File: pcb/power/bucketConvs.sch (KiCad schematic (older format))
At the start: 20 parts, among them U1 LM2840, U2 TS30012

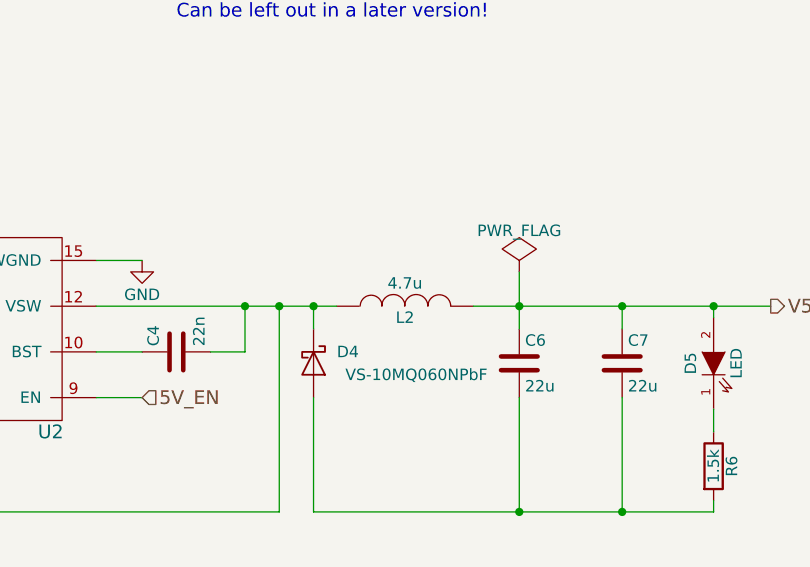
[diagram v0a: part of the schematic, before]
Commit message: Started placing some components.
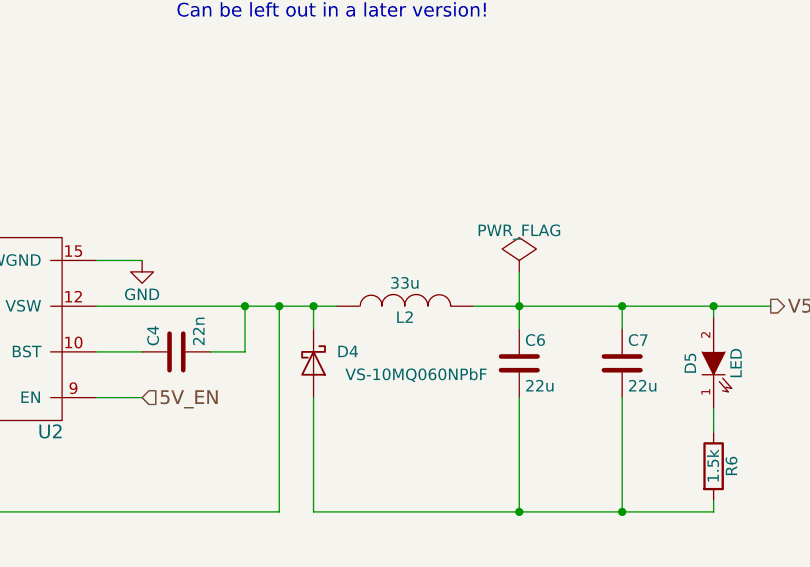
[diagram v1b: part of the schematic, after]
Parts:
- L2: value 4.7u -> 33u; footprint Additional:Taiyo_Yuden_NRS8030_IND -> Additional:Bourns_SRN3015; Digikey 587-2969-1-ND -> SRN3015-330MCT-ND
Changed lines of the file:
@@
 Text Notes 4250 4150 0    60   ~ 0
 Debugging Diode\n-----------------------\nDiode: 1.7 V, 2 mA\nP=2.161 mW\nCan be left out in a later version!
-Wire Wire Line
-	2800 2400 3700 2400
-Wire Wire Line
-	1800 2400 1800 2100
-Wire Wire Line
-	1800 2100 2150 2100
-Wire Wire Line
-	2450 2100 2850 2100
-Wire Wire Line
-	2850 2100 2850 2400
-Connection ~ 2850 2400
-Wire Wire Line
-	3650 1950 3650 2500
-Connection ~ 3650 2400
-Wire Wire Line
-	4350 2400 4350 2500
-Wire Wire Line
-	4350 2850 3650 2850
-Wire Wire Line
-	3650 2850 3650 2800
-Connection ~ 4350 2400
-Wire Wire Line
-	1700 2550 1800 2550
-Wire Wire Line
-	2800 2700 2900 2700
-Wire Wire Line
-	2900 2700 2900 2550
-Connection ~ 2900 2550
-Wire Wire Line
-	3000 3000 3000 3600
-Wire Wire Line
-	3000 2550 3000 2700
-Wire Wire Line
-	1800 3150 1800 3100
-Wire Wire Line
-	1800 2700 1800 2800
-Wire Wire Line
-	1800 2750 1600 2750
-Connection ~ 1800 2750
-Wire Wire Line
-	1200 2750 1200 1950
-Wire Wire Line
-	1200 1950 3650 1950
-Wire Wire Line
-	1200 2750 1300 2750
-Connection ~ 3000 3550
-Connection ~ 4350 2850
-Wire Wire Line
-	1800 3550 1800 3450
-Wire Wire Line
-	4350 3550 4350 2800
-Wire Wire Line
-	2800 2550 3150 2550
-Wire Wire Line
-	4800 2900 4800 2850
-Wire Wire Line
-	4800 3550 4800 3200
-Wire Wire Line
-	4800 2400 4800 2450
-Connection ~ 4350 3550
 $Comp
 L D_Schottky D2
@@
 	0    1    1    0
 $EndComp
-Connection ~ 3000 2550
 $Comp
 L GND #PWR09
@@
 	1    5750 5650
 	1    0    0    -1
-$EndComp
-$Comp
-L INDUCTOR L2
-U 1 1 5842F8BA
-P 5250 5400
-F 0 "L2" V 5200 5400 50  0000 C CNN
-F 1 "4.7u" V 5350 5400 50  0000 C CNN
-F 2 "Additional:Taiyo_Yuden_NRS8030_IND" H 5250 5400 50  0001 C CNN
-F 3 "http://www.yuden.co.jp/productdata/catalog/en/wound04_e.pdf" H 5250 5400 50  0001 C CNN
-F 4 "587-2969-1-ND " V 5250 5400 60  0001 C CNN "Digikey"
-	1    5250 5400
-	0    -1   -1   0
 $EndComp
 $Comp
@@
 Text Notes 4750 7050 0    60   ~ 0
 Debugging Diode\n-----------------------\nDiode: 1.7 V, 2 mA\nP=7.26 mW\nCan be left out in a later version!
-Wire Wire Line
-	1800 5250 1800 5200
-Connection ~ 1800 5200
-Wire Wire Line
-	1800 5550 1800 5650
-Connection ~ 1800 5600
-Wire Wire Line
-	3900 5400 4950 5400
-Connection ~ 5750 5400
-Wire Wire Line
-	4850 5500 4850 5400
-Connection ~ 4850 5400
-Wire Wire Line
-	5750 5250 5750 5500
-Wire Wire Line
-	6200 5400 6200 5500
-Wire Wire Line
-	4850 5800 4850 6300
-Wire Wire Line
-	6200 6300 6200 5800
-Wire Wire Line
-	5750 5800 5750 6300
-Connection ~ 5750 6300
-Wire Wire Line
-	1650 5200 2300 5200
-Wire Wire Line
-	2300 5400 2000 5400
-Wire Wire Line
-	2000 5400 2000 5600
-Wire Wire Line
-	2000 5600 1800 5600
-Wire Wire Line
-	3900 5600 4100 5600
-Connection ~ 4550 5400
-Wire Wire Line
-	2300 5600 2150 5600
-Wire Wire Line
-	2150 5600 2150 6300
-Wire Wire Line
-	4700 6300 4700 5400
-Connection ~ 4700 5400
-Connection ~ 6200 5400
-Wire Wire Line
-	4100 5800 3900 5800
-Wire Wire Line
-	4550 5600 4400 5600
-Wire Wire Line
-	6600 5850 6600 5950
-Wire Wire Line
-	6600 5400 6600 5450
 $Comp
 L TS30012 U2
@@
 	1    0    0    -1
 $EndComp
-Wire Wire Line
-	6600 6300 6600 6250
-Connection ~ 6200 6300
-Wire Wire Line
-	3900 5200 4100 5200
 Text Notes 1400 4900 0    60   ~ 0
 5V for Mobile Phone\n-----------------------\nVout,max=5 V\nAout,max = 2A
@@
 	1    0    0    -1
 $EndComp
-Wire Wire Line
-	4550 5400 4550 5600
 $Comp
 L PWR_FLAG #FLG012
@@
 Text HLabel 4100 5800 2    60   Input ~ 0
 5V_EN
-Wire Wire Line
-	5550 5400 6850 5400
 Text HLabel 6850 5400 2    60   Output ~ 0
 V5
+Text HLabel 5150 2400 2    60   Output ~ 0
+V28
+$Comp
+L INDUCTOR L2
+U 1 1 5846EBCA
+P 5250 5400
+F 0 "L2" V 5200 5400 50  0000 C CNN
+F 1 "33u" V 5350 5400 50  0000 C CNN
+F 2 "Additional:Bourns_SRN3015" H 5250 5400 50  0001 C CNN
+F 3 "http://www.bourns.com/docs/Product-Datasheets/SRN3015.pdf" H 5250 5400 50  0001 C CNN
+F 4 "SRN3015-330MCT-ND" V 5400 4850 60  0001 C CNN "Digikey"
+	1    5250 5400
+	0    -1   -1   0
+$EndComp
+Wire Wire Line
+	2800 2400 3700 2400
+Wire Wire Line
+	1800 2400 1800 2100
+Wire Wire Line
+	1800 2100 2150 2100
+Wire Wire Line
+	2450 2100 2850 2100
+Wire Wire Line
+	2850 2100 2850 2400
+Connection ~ 2850 2400
+Wire Wire Line
+	3650 1950 3650 2500
+Connection ~ 3650 2400
+Wire Wire Line
+	4350 2400 4350 2500
+Wire Wire Line
+	4350 2850 3650 2850
+Wire Wire Line
+	3650 2850 3650 2800
+Connection ~ 4350 2400
+Wire Wire Line
+	1700 2550 1800 2550
+Wire Wire Line
+	2800 2700 2900 2700
+Wire Wire Line
+	2900 2700 2900 2550
+Connection ~ 2900 2550
+Wire Wire Line
+	3000 3000 3000 3600
+Wire Wire Line
+	3000 2550 3000 2700
+Wire Wire Line
+	1800 3150 1800 3100
+Wire Wire Line
+	1800 2700 1800 2800
+Wire Wire Line
+	1800 2750 1600 2750
+Connection ~ 1800 2750
+Wire Wire Line
+	1200 2750 1200 1950
+Wire Wire Line
+	1200 1950 3650 1950
+Wire Wire Line
+	1200 2750 1300 2750
+Connection ~ 3000 3550
+Connection ~ 4350 2850
+Wire Wire Line
+	1800 3550 1800 3450
+Wire Wire Line
+	4350 3550 4350 2800
+Wire Wire Line
+	2800 2550 3150 2550
+Wire Wire Line
+	4800 2900 4800 2850
+Wire Wire Line
+	4800 3550 4800 3200
+Wire Wire Line
+	4800 2400 4800 2450
+Connection ~ 4350 3550
+Connection ~ 3000 2550
+Wire Wire Line
+	1800 5250 1800 5200
+Connection ~ 1800 5200
+Wire Wire Line
+	1800 5550 1800 5650
+Connection ~ 1800 5600
+Wire Wire Line
+	3900 5400 4950 5400
+Connection ~ 5750 5400
+Wire Wire Line
+	4850 5500 4850 5400
+Connection ~ 4850 5400
+Wire Wire Line
+	5750 5250 5750 5500
+Wire Wire Line
+	6200 5400 6200 5500
+Wire Wire Line
+	4850 5800 4850 6300
+Wire Wire Line
+	6200 6300 6200 5800
+Wire Wire Line
+	5750 5800 5750 6300
+Connection ~ 5750 6300
+Wire Wire Line
+	1650 5200 2300 5200
+Wire Wire Line
+	2300 5400 2000 5400
+Wire Wire Line
+	2000 5400 2000 5600
+Wire Wire Line
+	2000 5600 1800 5600
+Wire Wire Line
+	3900 5600 4100 5600
+Connection ~ 4550 5400
+Wire Wire Line
+	2300 5600 2150 5600
+Wire Wire Line
+	2150 5600 2150 6300
+Wire Wire Line
+	4700 6300 4700 5400
+Connection ~ 4700 5400
+Connection ~ 6200 5400
+Wire Wire Line
+	4100 5800 3900 5800
+Wire Wire Line
+	4550 5600 4400 5600
+Wire Wire Line
+	6600 5850 6600 5950
+Wire Wire Line
+	6600 5400 6600 5450
+Wire Wire Line
+	6600 6300 6600 6250
+Connection ~ 6200 6300
+Wire Wire Line
+	3900 5200 4100 5200
+Wire Wire Line
+	4550 5400 4550 5600
+Wire Wire Line
+	5550 5400 6850 5400
 Wire Wire Line
 	2150 6300 4700 6300
@@
 	4300 2400 5150 2400
 Connection ~ 6600 5400
-Text HLabel 5150 2400 2    60   Output ~ 0
-V28
 Connection ~ 4800 2400
 $EndSCHEMATC

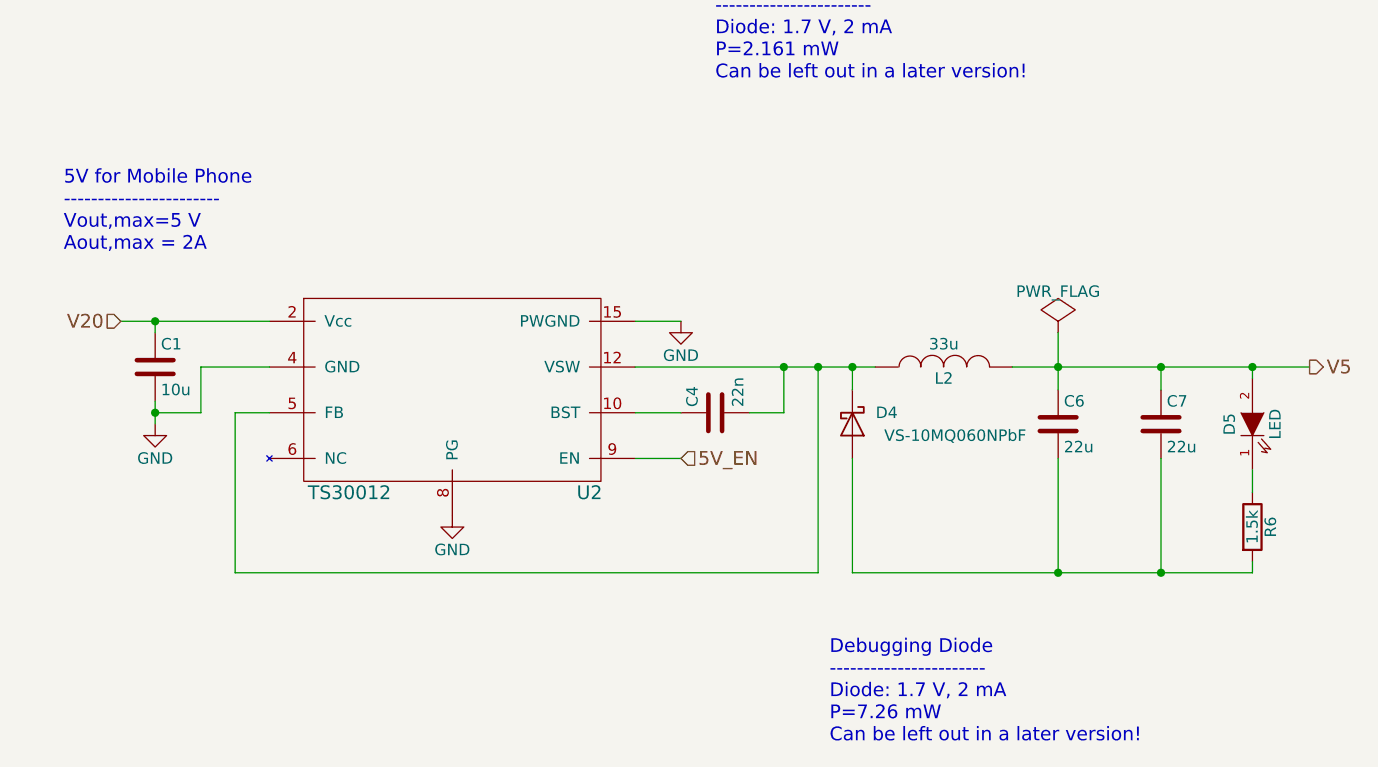
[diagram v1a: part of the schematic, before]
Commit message: Finished both bucket converters.
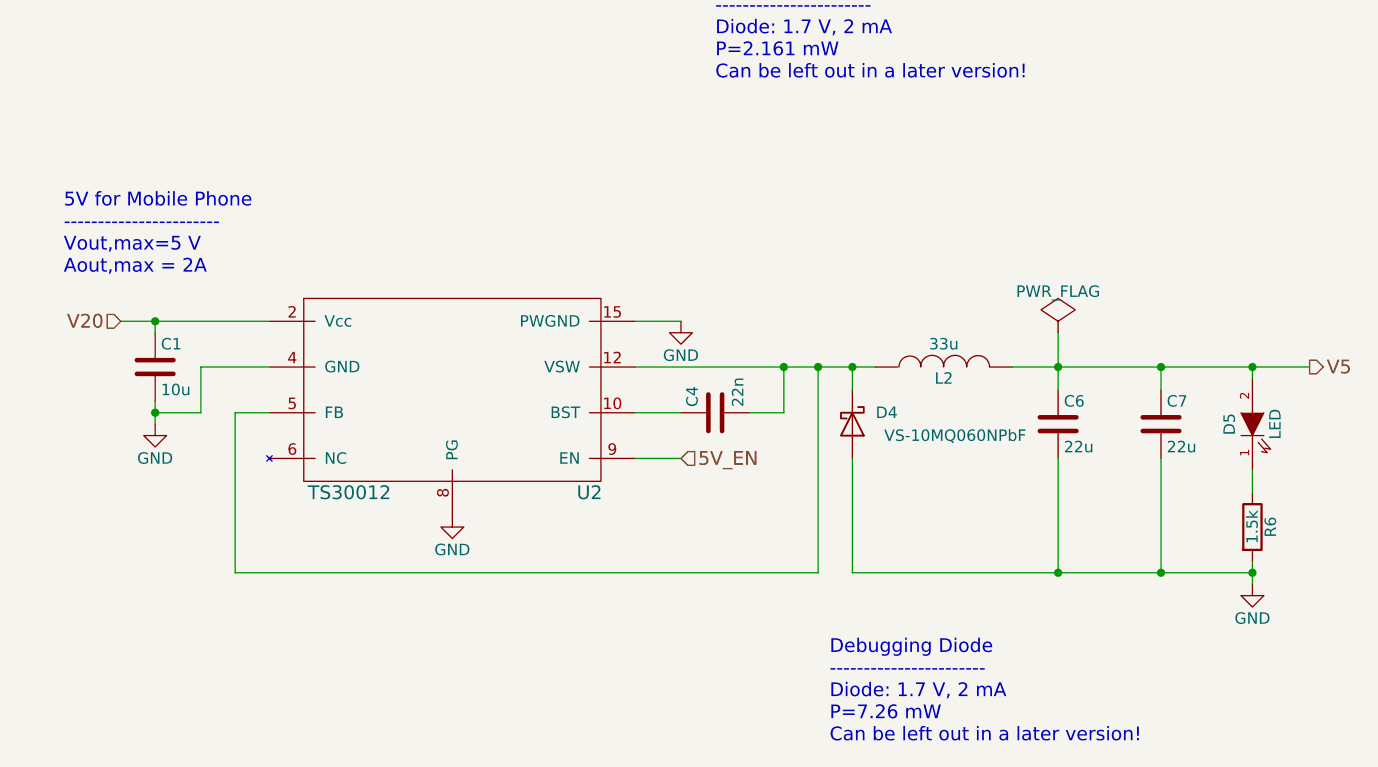
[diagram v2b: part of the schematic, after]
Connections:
- net GND: now also C6.2, C7.2, D4.2 (A), R6.2
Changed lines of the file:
@@
 	1    0    0    -1
 $EndComp
-Text Notes 1400 4900 0    60   ~ 0
+Text Notes 1400 5000 0    60   ~ 0
 5V for Mobile Phone\n-----------------------\nVout,max=5 V\nAout,max = 2A
 $Comp
@@
 	6600 5400 6600 5450
 Wire Wire Line
-	6600 6300 6600 6250
+	6600 6250 6600 6350
 Connection ~ 6200 6300
 Wire Wire Line
@@
 Connection ~ 6600 5400
 Connection ~ 4800 2400
+$Comp
+L GND #PWR?
+U 1 1 584C8E69
+P 6600 6350
+F 0 "#PWR?" H 6600 6100 50  0001 C CNN
+F 1 "GND" H 6600 6200 50  0000 C CNN
+F 2 "" H 6600 6350 50  0000 C CNN
+F 3 "" H 6600 6350 50  0000 C CNN
+	1    6600 6350
+	1    0    0    -1
+$EndComp
+Connection ~ 6600 6300
 $EndSCHEMATC

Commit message: Did a lot of stuff. Currently working on the exact 3D models for the headers.
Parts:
- R2, R3, R4, R5: footprint Resistors_SMD:R_0603_HandSoldering -> Additional:R_0603_HandSoldering_Same_As_C
- R6: footprint Capacitors_SMD:C_0603_HandSoldering -> Additional:R_0603_HandSoldering_Same_As_C
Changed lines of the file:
@@
 F 0 "R2" V 1530 2750 50  0000 C CNN
 F 1 "27k" V 1450 2750 50  0000 C CNN
-F 2 "Resistors_SMD:R_0603_HandSoldering" V 1380 2750 50  0001 C CNN
+F 2 "Additional:R_0603_HandSoldering_Same_As_C" V 1380 2750 50  0001 C CNN
 F 3 "http://industrial.panasonic.com/www-cgi/jvcr13pz.cgi?E+PZ+3+AOA0002+ERJ3EKF2702V+7+WW" H 1450 2750 50  0001 C CNN
 F 4 "P27.0KHCT-ND" V 1450 2750 60  0001 C CNN "Digikey"
@@
 F 0 "R3" V 1880 2950 50  0000 C CNN
 F 1 "10k" V 1800 2950 50  0000 C CNN
-F 2 "Resistors_SMD:R_0603_HandSoldering" V 1730 2950 50  0001 C CNN
+F 2 "Additional:R_0603_HandSoldering_Same_As_C" V 1730 2950 50  0001 C CNN
 F 3 "http://www.yageo.com.tw/exep/pages/download/literatures/PYu-R_INT-thick_7.pdf" H 1800 2950 50  0001 C CNN
 F 4 " 311-10.0KHRCT-ND" V 1800 2950 60  0001 C CNN "Digikey"
@@
 F 0 "R4" V 1880 3300 50  0000 C CNN
 F 1 "150" V 1800 3300 50  0000 C CNN
-F 2 "Resistors_SMD:R_0603_HandSoldering" V 1730 3300 50  0001 C CNN
+F 2 "Additional:R_0603_HandSoldering_Same_As_C" V 1730 3300 50  0001 C CNN
 F 3 "http://www.yageo.com.tw/exep/pages/download/literatures/PYu-R_INT-thick_7.pdf" H 1800 3300 50  0001 C CNN
 F 4 "311-150HRCT-ND" V 1800 3300 60  0001 C CNN "Digikey"
@@
 F 0 "R5" V 4880 3050 50  0000 C CNN
 F 1 "560R" V 4800 3050 50  0000 C CNN
-F 2 "Resistors_SMD:R_0603_HandSoldering" V 4730 3050 50  0001 C CNN
+F 2 "Additional:R_0603_HandSoldering_Same_As_C" V 4730 3050 50  0001 C CNN
 F 3 "http://www.yageo.com.tw/exep/pages/download/literatures/PYu-R_INT-thick_7.pdf" H 4800 3050 50  0001 C CNN
 F 4 "311-560GRCT-ND" V 4800 3050 60  0001 C CNN "Digikey"
@@
 F 0 "R6" V 6680 6100 50  0000 C CNN
 F 1 "1.5k" V 6600 6100 50  0000 C CNN
-F 2 "Capacitors_SMD:C_0603_HandSoldering" V 6530 6100 50  0001 C CNN
+F 2 "Additional:R_0603_HandSoldering_Same_As_C" V 6530 6100 50  0001 C CNN
 F 3 "http://www.yageo.com.tw/exep/pages/download/literatures/PYu-R_INT-thick_7.pdf" H 6600 6100 50  0001 C CNN
 F 4 "311-1.5KGRCT-ND " V 6600 6100 60  0001 C CNN "Digikey"
@@
 Connection ~ 4800 2400
 $Comp
-L GND #PWR?
+L GND #PWR013
 U 1 1 584C8E69
 P 6600 6350
-F 0 "#PWR?" H 6600 6100 50  0001 C CNN
+F 0 "#PWR013" H 6600 6100 50  0001 C CNN
 F 1 "GND" H 6600 6200 50  0000 C CNN
 F 2 "" H 6600 6350 50  0000 C CNN
